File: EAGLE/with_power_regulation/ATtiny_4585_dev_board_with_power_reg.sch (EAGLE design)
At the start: 19 parts, among them IC3 7805, J1 AVR_SPI_PRG_62X3_LOCK

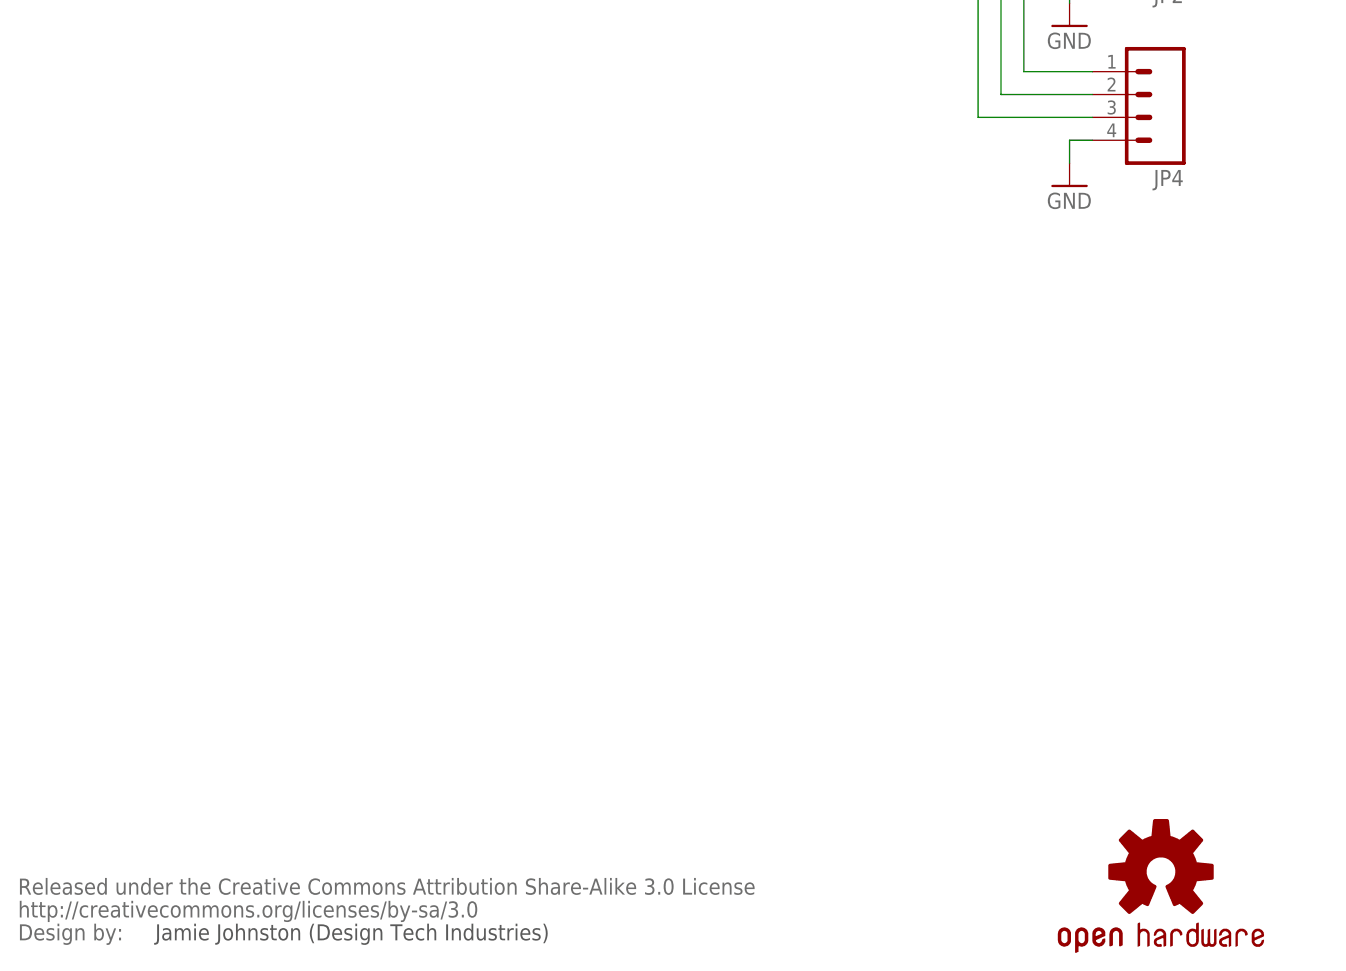
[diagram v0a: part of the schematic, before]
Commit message: Update of design files. Minor changes to thermocouple solder pads. New board images in 'docs' folder.
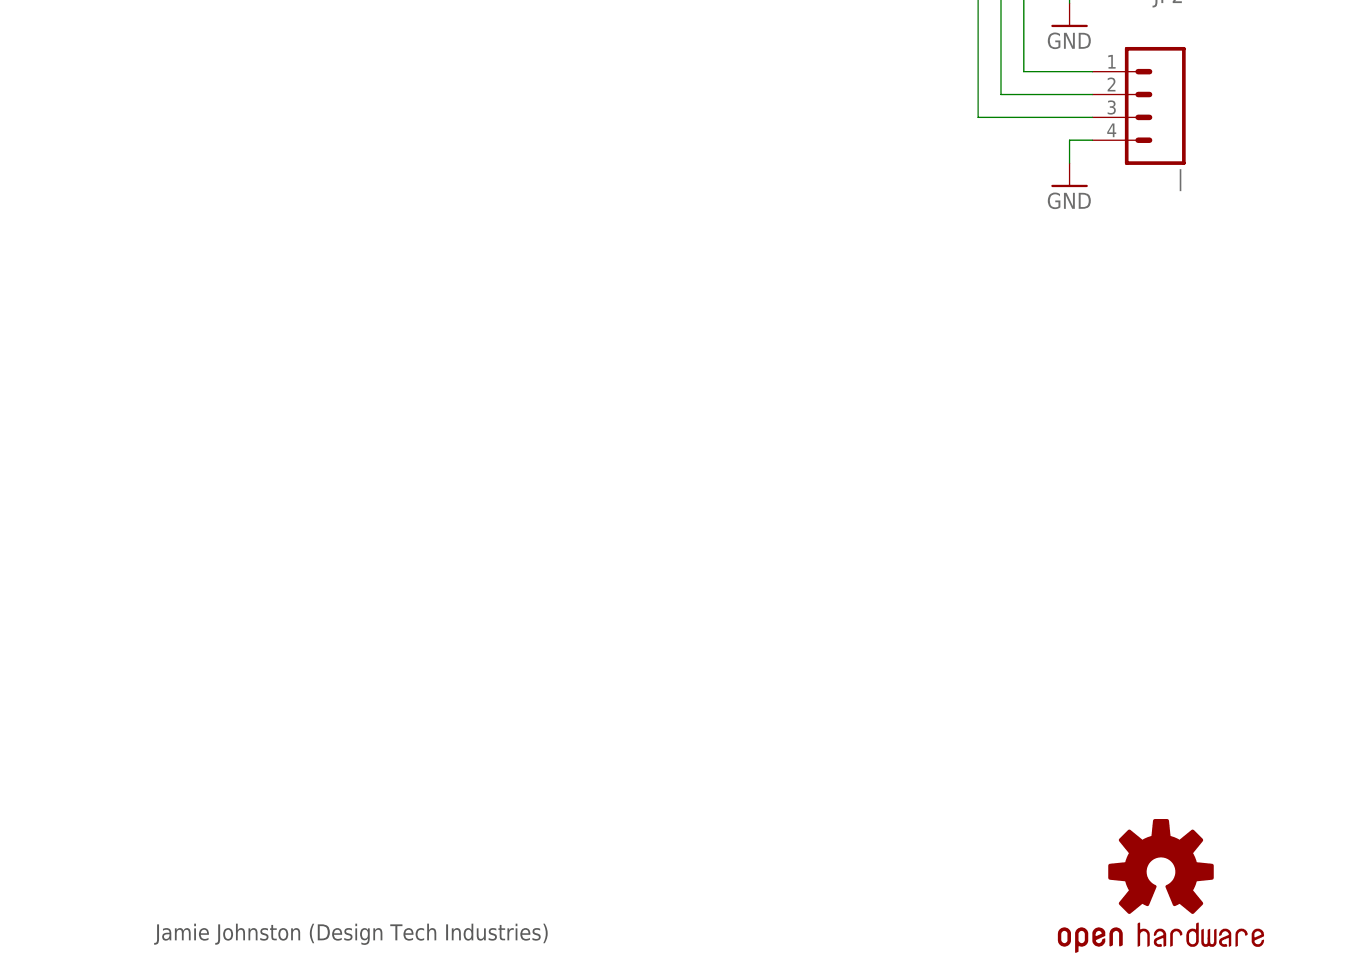
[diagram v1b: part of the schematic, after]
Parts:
- removed U$2: CREATIVE_COMMONS, SparkFun-Aesthetics:CREATIVE_COMMONS
- renumbered JP4 to |
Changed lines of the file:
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@@
 <part name="U$3" library="SparkFun-Aesthetics" deviceset="OSHW-LOGO" device="M"/>
 <part name="JP3" library="SparkFun" deviceset="M04" device="LOCK"/>
-<part name="JP4" library="SparkFun" deviceset="M04" device="LOCK"/>
+<part name="|" library="SparkFun" deviceset="M04" device="LOCK"/>
 <part name="GND2" library="SparkFun" deviceset="GND" device=""/>
 <part name="P+3" library="SparkFun" deviceset="VCC" device=""/>
-<part name="U$2" library="SparkFun-Aesthetics" deviceset="CREATIVE_COMMONS" device=""/>
 </parts>
 <sheets>
@@
 <instance part="U$3" gate="G$1" x="60.96" y="-38.1"/>
 <instance part="JP3" gate="G$1" x="58.42" y="109.22" rot="R180"/>
-<instance part="JP4" gate="G$1" x="58.42" y="48.26" rot="R180"/>
+<instance part="|" gate="G$1" x="58.42" y="48.26" rot="R180"/>
 <instance part="GND2" gate="1" x="50.8" y="38.1"/>
 <instance part="P+3" gate="1" x="50.8" y="114.3"/>
-<instance part="U$2" gate="G$1" x="-66.04" y="-45.72"/>
 </instances>
 <busses>
@@
 </segment>
 <segment>
-<pinref part="JP4" gate="G$1" pin="4"/>
+<pinref part="|" gate="G$1" pin="4"/>
 <wire x1="53.34" y1="43.18" x2="50.8" y2="43.18" width="0.1524" layer="91"/>
 <wire x1="50.8" y1="43.18" x2="50.8" y2="40.64" width="0.1524" layer="91"/>
@@
 <wire x1="-20.32" y1="104.14" x2="-20.32" y2="101.6" width="0.1524" layer="91"/>
 <junction x="-20.32" y="101.6"/>
-<pinref part="JP4" gate="G$1" pin="1"/>
+<pinref part="|" gate="G$1" pin="1"/>
 <wire x1="53.34" y1="50.8" x2="45.72" y2="50.8" width="0.1524" layer="91"/>
 <wire x1="45.72" y1="50.8" x2="45.72" y2="71.12" width="0.1524" layer="91"/>
@@
 <pinref part="U$1" gate="G$1" pin="PB3(ADC3)"/>
 <pinref part="JP2" gate="G$1" pin="2"/>
-<pinref part="JP4" gate="G$1" pin="2"/>
+<pinref part="|" gate="G$1" pin="2"/>
 <wire x1="53.34" y1="48.26" x2="43.18" y2="48.26" width="0.1524" layer="91"/>
 <wire x1="43.18" y1="48.26" x2="43.18" y2="76.2" width="0.1524" layer="91"/>
@@
 <pinref part="U$1" gate="G$1" pin="PB4(ADC2)"/>
 <pinref part="JP2" gate="G$1" pin="3"/>
-<pinref part="JP4" gate="G$1" pin="3"/>
+<pinref part="|" gate="G$1" pin="3"/>
 <wire x1="53.34" y1="45.72" x2="40.64" y2="45.72" width="0.1524" layer="91"/>
 <wire x1="40.64" y1="45.72" x2="40.64" y2="73.66" width="0.1524" layer="91"/>
